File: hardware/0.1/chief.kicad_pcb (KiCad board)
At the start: 2 copper layers, 84.3 x 65 mm, 60 parts, among them J1 USB_C_Receptacle_USB2.0, Q1 DTC123J, Q2 BSS138, SW1 Encoder_MX_RGB, SW10 Encoder_MX_RGB, SW11 MX_RGB, SW12 MX_RGB, SW13 SW_Push, SW2 MX_RGB, SW3 MX_RGB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

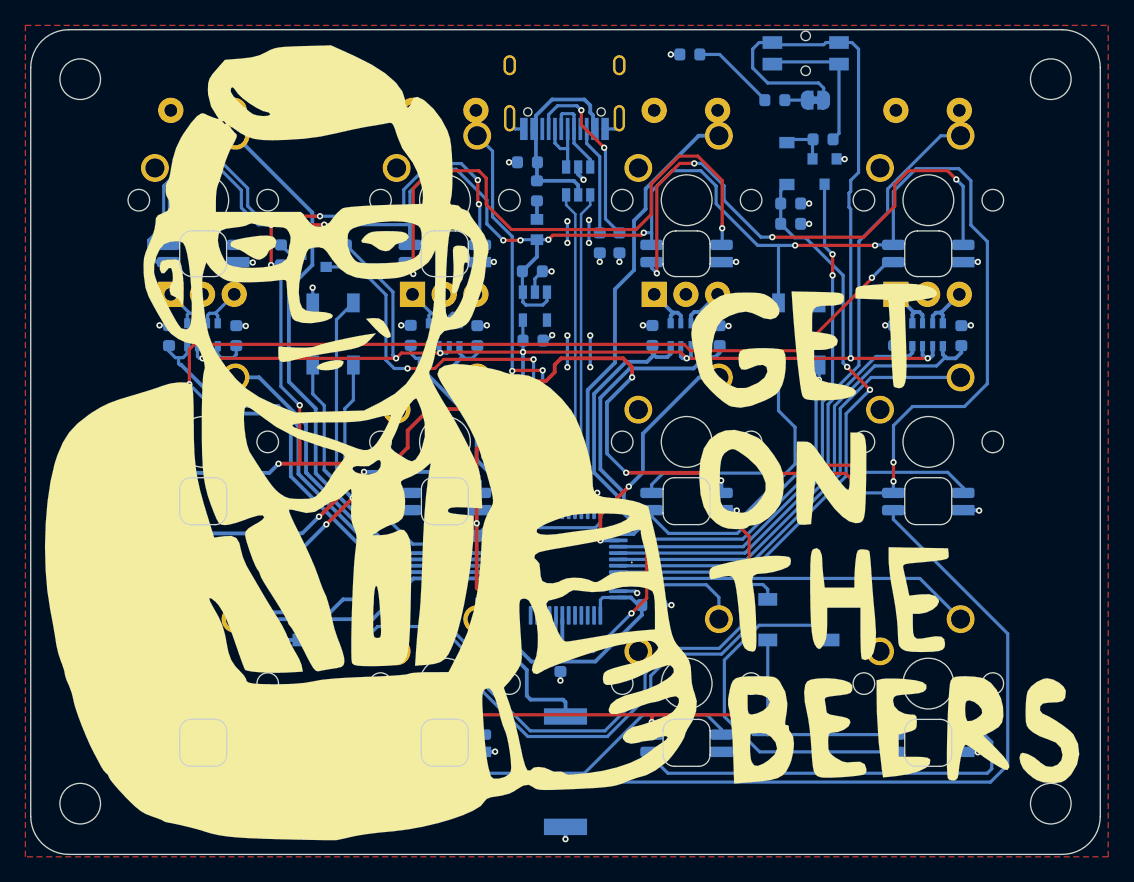
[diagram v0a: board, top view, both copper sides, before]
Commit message: thumb fix, LED position adjusted and rewired
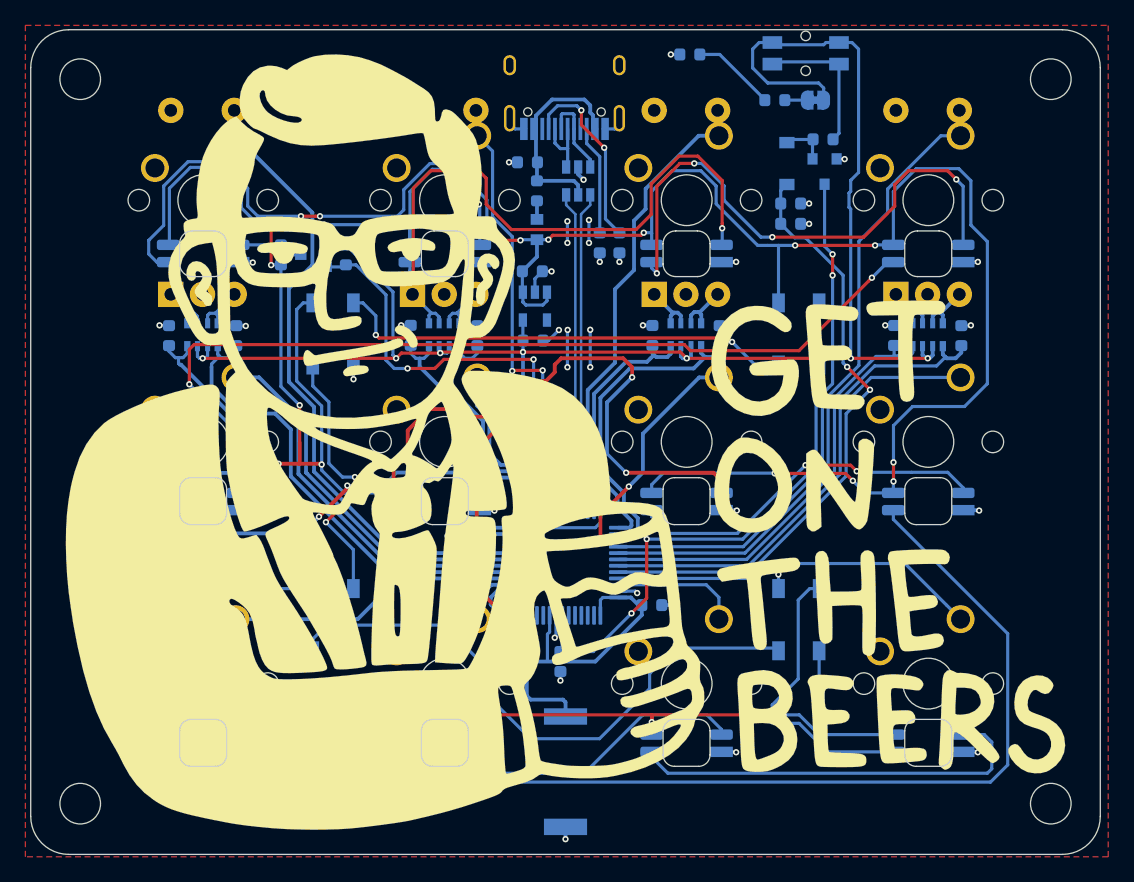
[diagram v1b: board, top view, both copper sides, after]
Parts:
- moved D4 22.5 mm to (124.5, 104.5), turned to 270 degrees
- moved D5 22.5 mm to (124.5, 82.0), turned to 270 degrees
- moved H5 0.34 mm to (142.8, 90.4)
- turned D3 to 90 degrees
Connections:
- D6 pad 2: (no net) -> Net-(D6-Pad2)
- J1 pad A8: (no net) -> Net-(J1-PadA8)
- J1 pad B8: (no net) -> Net-(J1-PadB8)
- U1 pad 4: (no net) -> Net-(U1-Pad4)
- U3 pad 10: (no net) -> Net-(U3-Pad10)
- U3 pad 11: (no net) -> Net-(U3-Pad11)
- U3 pad 12: (no net) -> Net-(U3-Pad12)
- U3 pad 13: (no net) -> Net-(U3-Pad13)
- U3 pad 2: (no net) -> Net-(U3-Pad2)
- U3 pad 21: (no net) -> Net-(U3-Pad21)
- U3 pad 22: (no net) -> Net-(U3-Pad22)
- U3 pad 3: (no net) -> Net-(U3-Pad3)
- U3 pad 30: (no net) -> Net-(U3-Pad30)
- U3 pad 31: (no net) -> Net-(U3-Pad31)
- U3 pad 4: (no net) -> Net-(U3-Pad4)
- U3 pad 5: (no net) -> Net-(U3-Pad5)
- U3 pad 6: (no net) -> Net-(U3-Pad6)
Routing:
- net Net-(D5-Pad2): track 63.3 -> 36.4 mm
- net Net-(D3-Pad2): track 68.4 -> 46.8 mm, vias 2 -> 0
- net /BKLT: track 28.9 -> 22.8 mm
- net /SW12: track 28.3 -> 29.3 mm
- net +5V: track 315.6 -> 316.3 mm
- net GND: track 56.7 -> 56.9 mm, vias 50 -> 49

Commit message: Fix 1 unconnected ground
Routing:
- net GND: track 56.9 -> 58.1 mm, vias 49 -> 50

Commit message: off to fab
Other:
- board text added: "JLCJLCJLC"
